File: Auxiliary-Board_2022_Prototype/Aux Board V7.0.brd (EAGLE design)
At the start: 114.3 x 96.6 mm, 46 parts, among them CON11 1X01, CON12 1X01, CON13 1X01, CON14 1X01, CON15 1X01, CON16 1X01, CON17 1X01, CON18 1X01, CON5 1X01, CON8 1X01

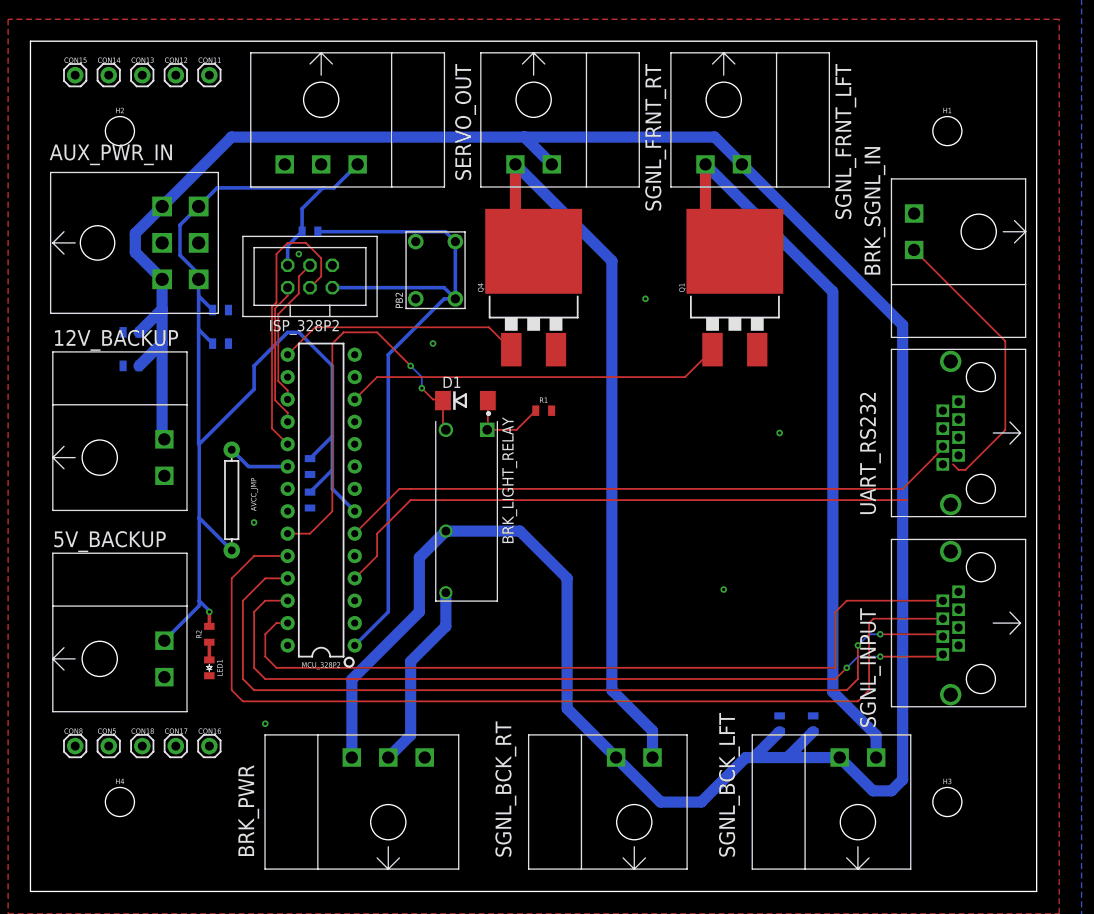
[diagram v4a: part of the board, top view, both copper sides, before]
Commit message: feat: converted SGNL switch method from MOSTFETs to Relays
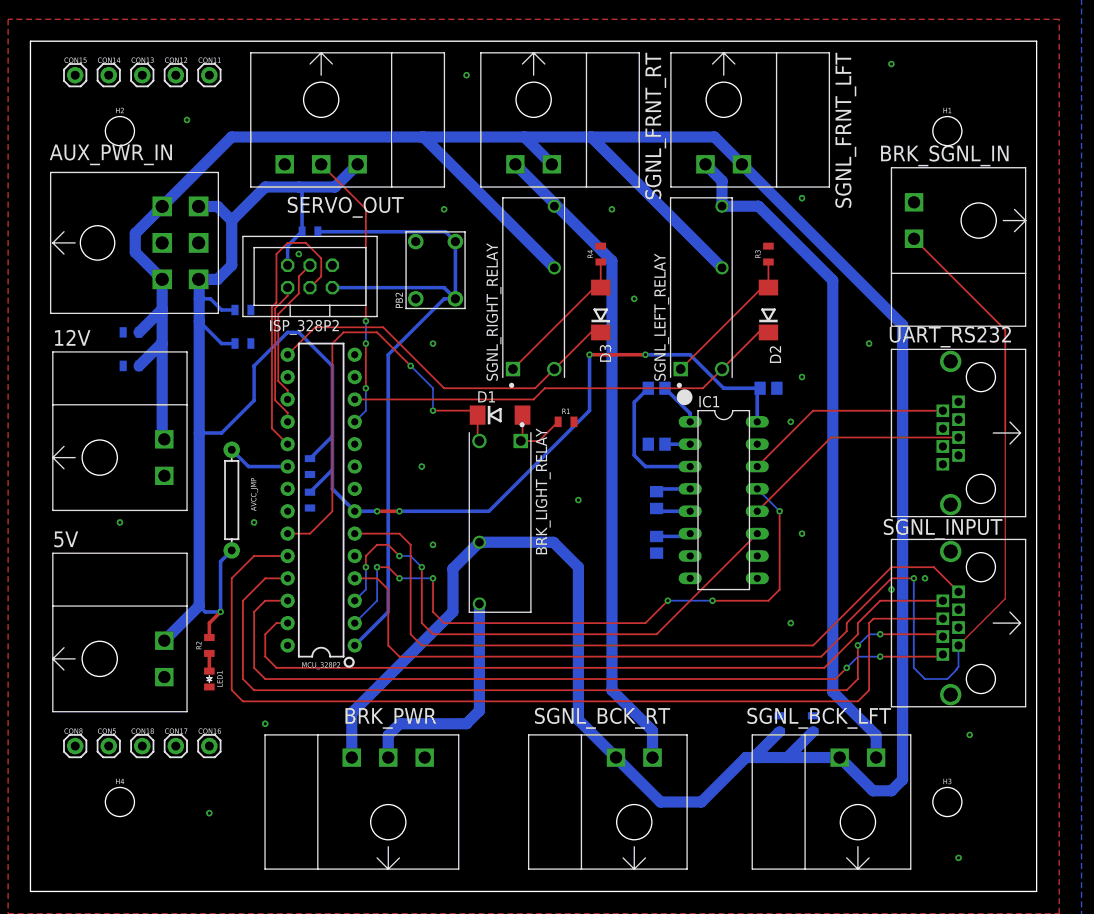
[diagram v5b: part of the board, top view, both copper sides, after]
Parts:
- removed Q1, Q4: (no value), EcoCar-Discrete-Semiconductors:TO-263/D2PAK
- added C10, C11, C12, C13, C9: 0.1µF, rcl:C0805
- added D2, D3: (no value), EcoCar-Discrete-Semiconductors:DO214AA
- added IC1: RS232-TTL_MAX232E, EcoCar-Integrated-Circuits:DIP16
- added R3, R4: 1K, EcoCar-Passives:0805
- added SGNL_LEFT_RELAY, SGNL_RIGHT_RELAY: RELAY_SPST-NO_3A, EcoCar-Electromechanical:TE_1-1721081-2
- moved D1 4.27 mm to (53.3, 59.2)
- moved BRK_LIGHT_RELAY 4.02 mm to (53.3, 47.0)
- moved R1 2.84 mm to (60.8, 58.4)
- moved C3 2.54 mm to (24.1, 71.1)
- moved C4 2.54 mm to (24.1, 67.3)
- moved LED1 1.27 mm to (20.3, 29.2)
- moved BRK_SGNL_IN 1.27 mm to (113.0, 81.3)
- moved R2 1.27 mm to (20.3, 33.0)
- renumbered 12V_BACKUP to 12V, 5V_BACKUP to 5V
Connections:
- removed net SERVO_O/P: MCU_328P2.28, SERVO_OUT.2
- new net N$10: C10.1, IC1.4
- new net N$11: C11.1, IC1.2
- new net N$12: C12.2, IC1.6
- new net N$13: D2.A, R3.1, SGNL_LEFT_RELAY.1
- new net N$14: D3.A, R4.1, SGNL_RIGHT_RELAY.1
- new net N$6: C9.2, IC1.3
- new net N$7: C10.2, IC1.5
- new net N$9: C9.1, IC1.1
- new net RX: IC1.13, MCU_328P2.2
- new net SERVO_PWM_O/P: MCU_328P2.11, SERVO_OUT.2
- new net TX: IC1.11, MCU_328P2.3
- net 12V: now also SGNL_LEFT_RELAY.3, SGNL_RIGHT_RELAY.3
- net 5V: now also C13.1, IC1.16
- net GND: now also C11.2, C12.1, C13.2, IC1.15, R3.2, R4.2, SGNL_INPUT.3, SGNL_INPUT.5; no longer Q1.3, Q4.3
- net RS_RX: now also IC1.12
- net RS_TX: now also IC1.14
- net SGNL_LEFT_12V: now also SGNL_LEFT_RELAY.4; no longer Q1.2
- net SGNL_LEFT_O/P: now also D2.C, SGNL_LEFT_RELAY.2; no longer Q1.1
- net SGNL_RIGHT_12V: now also SGNL_RIGHT_RELAY.4; no longer Q4.2
- net SGNL_RIGHT_O/P: now also D3.C, SGNL_RIGHT_RELAY.2; no longer Q4.1
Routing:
- net 5V: track 144.6 -> 217.8 mm, vias 1 -> 5
- net RX: track 0.00 -> 72.0 mm, vias 0 -> 6
- net TX: track 0.00 -> 63.2 mm, vias 0 -> 3
- net BRK_I/P: track 100.7 -> 146.6 mm, vias 0 -> 1
- net 12V: track 304.9 -> 344.4 mm
- net SERVO_PWM_O/P: track 0.00 -> 31.9 mm, vias 0 -> 3
- net RS_RX: track 0.00 -> 26.3 mm
- net RS_TX: track 0.00 -> 23.7 mm
- net N$14: track 0.00 -> 16.7 mm
- net N$13: track 0.00 -> 16.7 mm
- net N$6: track 0.00 -> 15.2 mm
- net SGNL_RIGHT_O/P: track 27.7 -> 42.3 mm
- net HAZARD_I/P: track 70.8 -> 84.6 mm
- net SGNL_RIGHT_12V: track 84.6 -> 74.1 mm
- net SGNL_LEFT_O/P: track 43.0 -> 50.1 mm
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
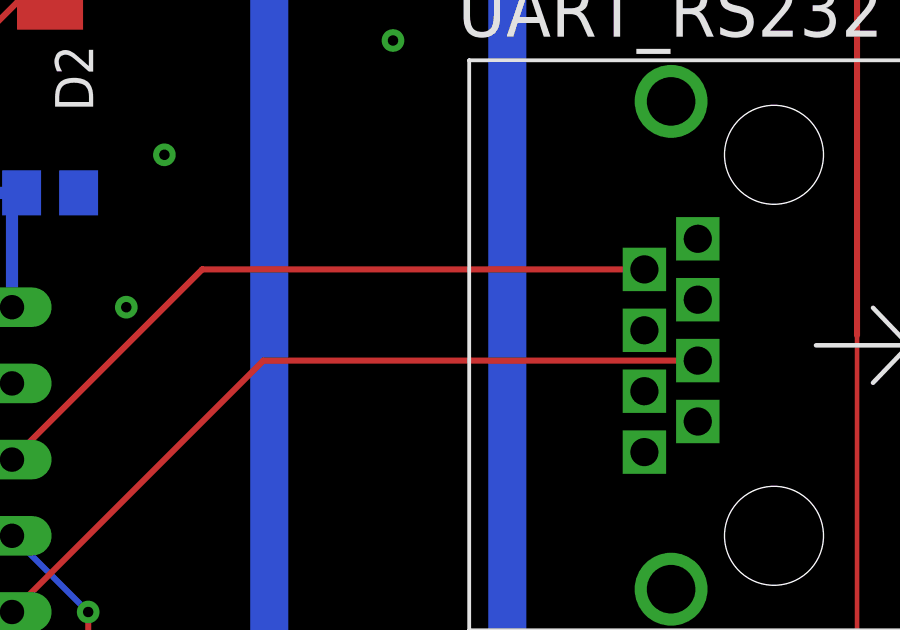
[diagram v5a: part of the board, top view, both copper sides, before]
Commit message: fix: correct RS232 pins
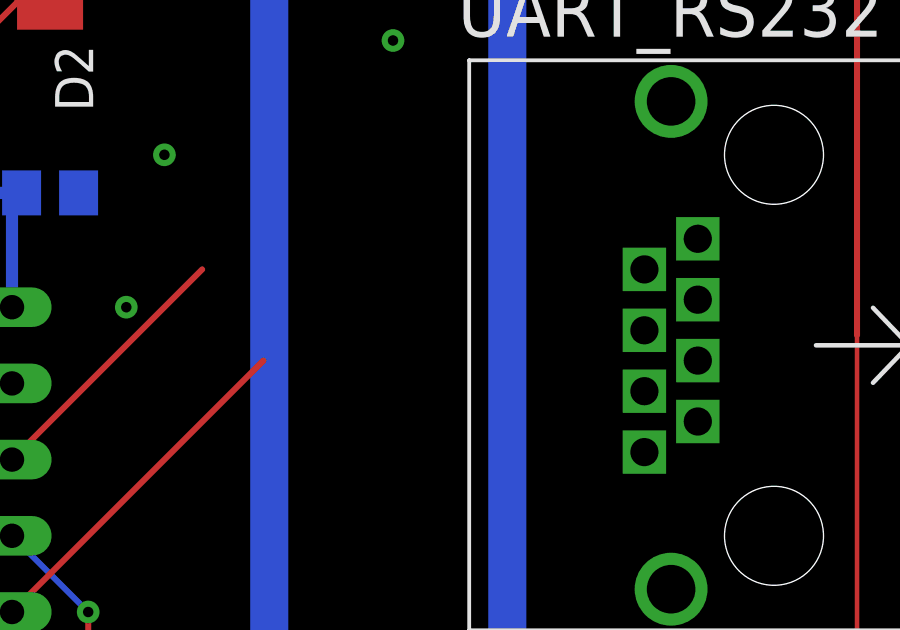
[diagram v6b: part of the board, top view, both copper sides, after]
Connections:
- net GND: now also UART_RS232.5; no longer UART_RS232.3
- net RS_RX: now also UART_RS232.3; no longer UART_RS232.5
- net RS_TX: now also UART_RS232.6; no longer UART_RS232.2
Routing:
- net RS_TX: track 23.7 -> 8.97 mm
- net RS_RX: track 26.3 -> 11.9 mm
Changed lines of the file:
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@@
 <contactref element="C4" pad="1"/>
 <contactref element="C8" pad="1"/>
-<contactref element="UART_RS232" pad="3"/>
-<contactref element="UART_RS232" pad="4"/>
 <contactref element="IC1" pad="15"/>
 <contactref element="C11" pad="2"/>
@@
 <via x="87.63" y="63.5" extent="1-16" drill="0.35"/>
 <via x="45.72" y="67.31" extent="1-16" drill="0.35"/>
+<contactref element="UART_RS232" pad="4"/>
+<contactref element="UART_RS232" pad="5"/>
+<wire x1="83.82" y1="78.37" x2="100.36" y2="83.35" width="0" layer="19" extent="1-1"/>
+<wire x1="87.63" y1="63.5" x2="83.82" y2="78.37" width="0" layer="19" extent="1-1"/>
+<wire x1="84.77" y1="62.23" x2="87.63" y2="63.5" width="0" layer="19" extent="16-16"/>
+<wire x1="82.55" y1="55.88" x2="84.77" y2="62.23" width="0" layer="19" extent="16-16"/>
+<wire x1="70.17" y1="55.88" x2="82.55" y2="55.88" width="0" layer="19" extent="16-16"/>
+<wire x1="61.733" y1="58.42" x2="70.17" y2="55.88" width="0" layer="19" extent="1-16"/>
+<wire x1="71.12" y1="43.5" x2="70.17" y2="55.88" width="0" layer="19" extent="16-16"/>
+<wire x1="68.58" y1="72.39" x2="61.733" y2="58.42" width="0" layer="19" extent="1-1"/>
+<wire x1="64.77" y1="78.37" x2="68.58" y2="72.39" width="0" layer="19" extent="1-1"/>
+<wire x1="104.52" y1="65.28" x2="87.63" y2="63.5" width="0" layer="19" extent="1-1"/>
+<wire x1="103.63" y1="57.65" x2="104.52" y2="65.28" width="0" layer="19" extent="1-1"/>
+<wire x1="105.41" y1="56.64" x2="103.63" y2="57.65" width="0" layer="19" extent="1-1"/>
+<wire x1="104.52" y1="49.02" x2="105.41" y2="56.64" width="0" layer="19" extent="1-1"/>
+<wire x1="104.52" y1="43.69" x2="104.52" y2="49.02" width="0" layer="19" extent="1-1"/>
+<wire x1="101.6" y1="40.64" x2="104.52" y2="43.69" width="0" layer="19" extent="1-1"/>
+<wire x1="97.79" y1="39.37" x2="101.6" y2="40.64" width="0" layer="19" extent="1-1"/>
+<wire x1="105.41" y1="37.08" x2="101.6" y2="40.64" width="0" layer="19" extent="1-1"/>
+<wire x1="105.41" y1="35.05" x2="105.41" y2="37.08" width="0" layer="19" extent="1-1"/>
+<wire x1="104.52" y1="27.43" x2="105.41" y2="35.05" width="0" layer="19" extent="1-1"/>
+<wire x1="86.36" y1="35.56" x2="97.79" y2="39.37" width="0" layer="19" extent="1-1"/>
+<wire x1="85.09" y1="25.03" x2="86.36" y2="35.56" width="0" layer="19" extent="16-16"/>
+<wire x1="88.9" y1="25.03" x2="85.09" y2="25.03" width="0" layer="19" extent="16-16"/>
+<wire x1="45.72" y1="67.31" x2="61.733" y2="58.42" width="0" layer="19" extent="1-1"/>
+<wire x1="43.76" y1="72.39" x2="45.72" y2="67.31" width="0" layer="19" extent="1-1"/>
+<wire x1="43.76" y1="78.89" x2="43.76" y2="72.39" width="0" layer="19" extent="1-1"/>
+<wire x1="34.29" y1="76.2" x2="43.76" y2="78.89" width="0" layer="19" extent="1-1"/>
+<wire x1="30.48" y1="77.47" x2="34.29" y2="76.2" width="0" layer="19" extent="1-1"/>
+<wire x1="25.03" y1="71.12" x2="30.48" y2="77.47" width="0" layer="19" extent="16-16"/>
+<wire x1="25.03" y1="67.31" x2="25.03" y2="71.12" width="0" layer="19" extent="16-16"/>
+<wire x1="19.1" y1="78.74" x2="25.03" y2="71.12" width="0" layer="19" extent="16-16"/>
+<wire x1="14.96" y1="78.74" x2="19.1" y2="78.74" width="0" layer="19" extent="1-1"/>
+<wire x1="28.88" y1="87.66" x2="30.48" y2="77.47" width="0" layer="19" extent="1-1"/>
+<wire x1="10.53" y1="68.58" x2="14.96" y2="78.74" width="0" layer="19" extent="16-16"/>
+<wire x1="10.53" y1="64.77" x2="10.53" y2="68.58" width="0" layer="19" extent="16-16"/>
+<wire x1="15.21" y1="52.286" x2="10.53" y2="64.77" width="0" layer="19" extent="16-16"/>
+<wire x1="25.4" y1="46.99" x2="15.21" y2="52.286" width="0" layer="19" extent="1-1"/>
+<wire x1="29.21" y1="48.26" x2="25.4" y2="46.99" width="0" layer="19" extent="1-1"/>
+<wire x1="31.75" y1="48.63" x2="29.21" y2="48.26" width="0" layer="19" extent="16-16"/>
+<wire x1="31.75" y1="52.44" x2="31.75" y2="48.63" width="0" layer="19" extent="16-16"/>
+<wire x1="36.83" y1="50.8" x2="31.75" y2="52.44" width="0" layer="19" extent="16-16"/>
+<wire x1="20.32" y1="28.31" x2="25.4" y2="46.99" width="0" layer="19" extent="1-1"/>
+<wire x1="15.21" y1="29.426" x2="20.32" y2="28.31" width="0" layer="19" extent="1-1"/>
+<wire x1="26.67" y1="24.13" x2="20.32" y2="28.31" width="0" layer="19" extent="1-1"/>
+<wire x1="44.78" y1="20.29" x2="26.67" y2="24.13" width="0" layer="19" extent="1-1"/>
 </signal>
 <signal name="12V">
@@
 </signal>
 <signal name="RS_TX">
-<contactref element="UART_RS232" pad="2"/>
 <contactref element="IC1" pad="14"/>
 <wire x1="82.55" y1="53.34" x2="88.89" y2="59.68" width="0.2032" layer="1"/>
-<wire x1="88.89" y1="59.68" x2="103.63" y2="59.68" width="0.2032" layer="1"/>
+<contactref element="UART_RS232" pad="6"/>
+<wire x1="88.89" y1="59.68" x2="103.63" y2="55.62" width="0" layer="19" extent="1-1"/>
 </signal>
 <signal name="RS_RX">
-<contactref element="UART_RS232" pad="5"/>
 <contactref element="IC1" pad="12"/>
 <wire x1="82.55" y1="48.26" x2="90.93" y2="56.64" width="0.2032" layer="1"/>
-<wire x1="90.93" y1="56.64" x2="105.41" y2="56.64" width="0.2032" layer="1"/>
+<contactref element="UART_RS232" pad="3"/>
+<wire x1="90.93" y1="56.64" x2="105.41" y2="58.67" width="0" layer="19" extent="1-1"/>
 </signal>
 <signal name="RX">
